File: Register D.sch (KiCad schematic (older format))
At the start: 2 parts

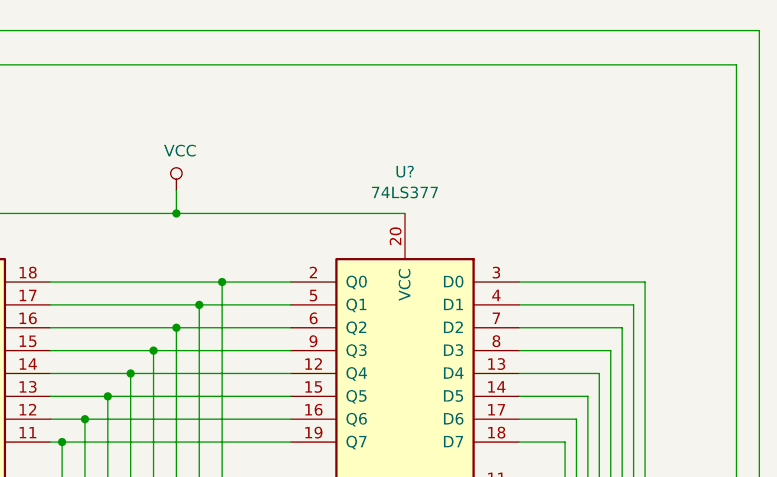
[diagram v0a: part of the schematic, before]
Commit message: Some of these chips actually need to be 74F not 74LS.
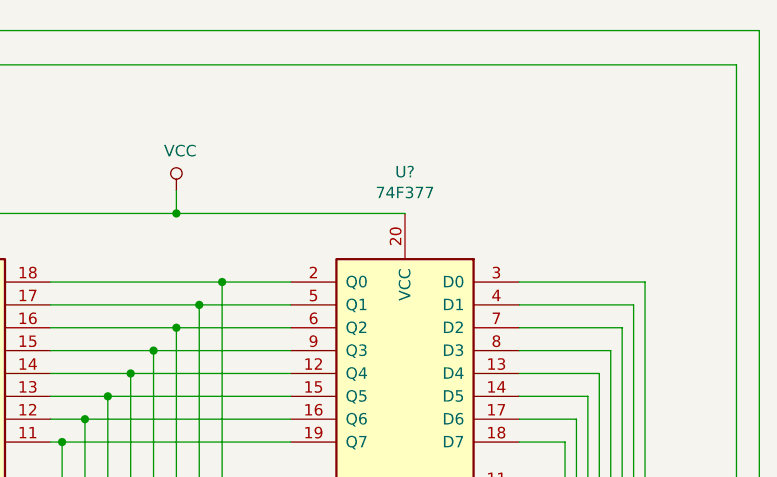
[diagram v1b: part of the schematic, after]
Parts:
- U?: value 74LS377 -> 74F377
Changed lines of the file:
@@
 AR Path="/5D29E36D/5D2A25F1" Ref="U?"  Part="1"
 F 0 "U?" H 7450 4331 50  0000 C CNN
-F 1 "74LS377" H 7450 4240 50  0000 C CNN
+F 1 "74F377" H 7450 4240 50  0000 C CNN
 F 2 "" H 7450 3350 50  0001 C CNN
 F 3 "http://www.ti.com/lit/gpn/sn74LS377" H 7450 3350 50  0001 C CNN
